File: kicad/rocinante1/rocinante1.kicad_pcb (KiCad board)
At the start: 4 copper layers, 150 x 100 mm, 142 parts, among them J1 ESP_01, J10 KEYBOARD, J11 SERIAL, J12 SD_Card, J13 USBFS/POWER, J14 I2S, J15 NEOPIXEL, J16 EXPHDR, J2 SWD, J3 COMPOSITE, J4 CTRL1, J5 CTRL2, J6 VGA, J7 AUDIOIN, J8 AUDIOOUT, J9 MOUSE, Q1 Q_NPN_CBE, SW1 RESET, SW2 USER1, SW3 USER2, SW4 USER3, SW5 BOOT0, U1 STM32H743IITx, U2 W9812G6KH-6, U3 LD1117S33TR_SOT223, X1 ASE-14.31818MHz, Y1 25MHz

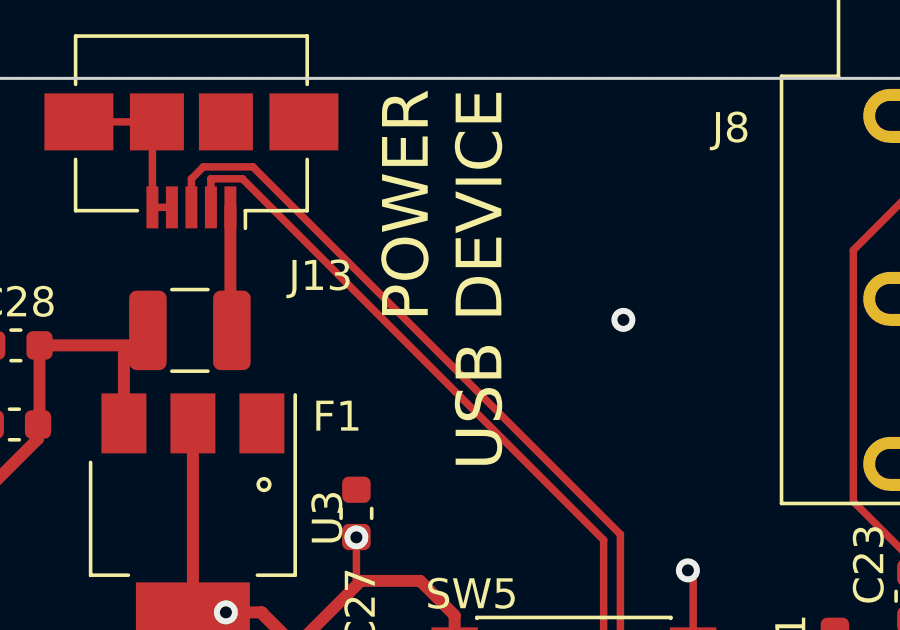
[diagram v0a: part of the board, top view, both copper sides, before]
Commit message: fix cap at composite out
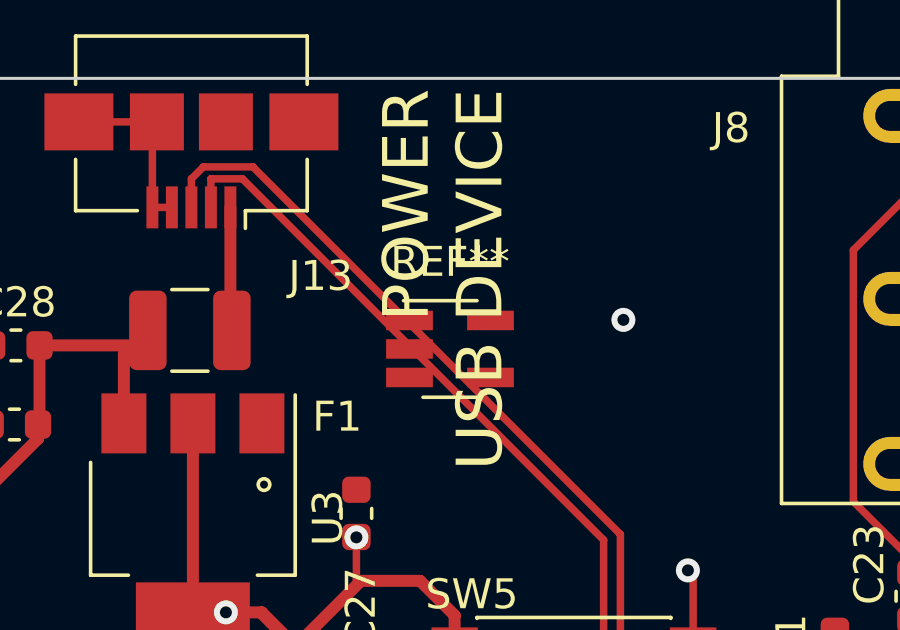
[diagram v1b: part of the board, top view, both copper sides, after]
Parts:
- added REF**: SOT-23-5_HandSoldering, Package_TO_SOT_SMD:SOT-23-5_HandSoldering, F.Cu at (84.0, 52.3)
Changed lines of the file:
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@@
     (tracks 3776)
     (zones 0)
-    (modules 142)
+    (modules 143)
     (nets 190)
   )
@@
     (add_net VREFP)
   )
+  (module Package_TO_SOT_SMD:SOT-23-5_HandSoldering (layer F.Cu)
+    (at 83.97 52.32)
+    (descr "5-pin SOT23 package")
+    (tags "SOT-23-5 hand-soldering")
+    (attr smd)
+    (fp_text reference REF** (at 0 -2.9) (layer F.SilkS)
+      (effects (font (size 1 1) (thickness 0.15)))
+    )
+    (fp_text value SOT-23-5_HandSoldering (at 0 2.9) (layer F.Fab)
+      (effects (font (size 1 1) (thickness 0.15)))
+    )
+    (fp_line (start 2.38 1.8) (end -2.38 1.8) (layer F.CrtYd) (width 0.05))
+    (fp_line (start 2.38 1.8) (end 2.38 -1.8) (layer F.CrtYd) (width 0.05))
+    (fp_line (start -2.38 -1.8) (end -2.38 1.8) (layer F.CrtYd) (width 0.05))
+    (fp_line (start -2.38 -1.8) (end 2.38 -1.8) (layer F.CrtYd) (width 0.05))
+    (fp_line (start 0.9 -1.55) (end 0.9 1.55) (layer F.Fab) (width 0.1))
+    (fp_line (start 0.9 1.55) (end -0.9 1.55) (layer F.Fab) (width 0.1))
+    (fp_line (start -0.9 -0.9) (end -0.9 1.55) (layer F.Fab) (width 0.1))
+    (fp_line (start 0.9 -1.55) (end -0.25 -1.55) (layer F.Fab) (width 0.1))
+    (fp_line (start -0.9 -0.9) (end -0.25 -1.55) (layer F.Fab) (width 0.1))
+    (fp_line (start 0.9 -1.61) (end -1.55 -1.61) (layer F.SilkS) (width 0.12))
+    (fp_line (start -0.9 1.61) (end 0.9 1.61) (layer F.SilkS) (width 0.12))
+    (fp_text user %R (at 0 0 90) (layer F.Fab)
+      (effects (font (size 0.5 0.5) (thickness 0.075)))
+    )
+    (pad 5 smd rect (at 1.35 -0.95) (size 1.56 0.65) (layers F.Cu F.Paste F.Mask))
+    (pad 4 smd rect (at 1.35 0.95) (size 1.56 0.65) (layers F.Cu F.Paste F.Mask))
+    (pad 3 smd rect (at -1.35 0.95) (size 1.56 0.65) (layers F.Cu F.Paste F.Mask))
+    (pad 2 smd rect (at -1.35 0) (size 1.56 0.65) (layers F.Cu F.Paste F.Mask))
+    (pad 1 smd rect (at -1.35 -0.95) (size 1.56 0.65) (layers F.Cu F.Paste F.Mask))
+    (model ${KISYS3DMOD}/Package_TO_SOT_SMD.3dshapes/SOT-23-5.wrl
+      (at (xyz 0 0 0))
+      (scale (xyz 1 1 1))
+      (rotate (xyz 0 0 0))
+    )
+  )
   (module Package_TO_SOT_SMD:SOT-323_SC-70 (layer F.Cu)
